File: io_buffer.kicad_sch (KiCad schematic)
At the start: 68 parts, among them J15 Conn_01x08, J5 IDC-Header_2x10_P2.54mm, J6 Conn_01x08, U13 SN74LVC1T45DCKR, U14 SN74LVC1T45DCKR, U15 SN74LVC1T45DCKR, U16 SN74LVC1T45DCKR, U17 SN74LVC1T45DCKR, U18 PCA6408APW, U19 TPS73101DBV, U20 DAC081C081CIMK, U21 INA233, U6 SN74LVC1T45DCKR, U7 SN74LVC1T45DCKR, U8 SN74LVC1T45DCKR

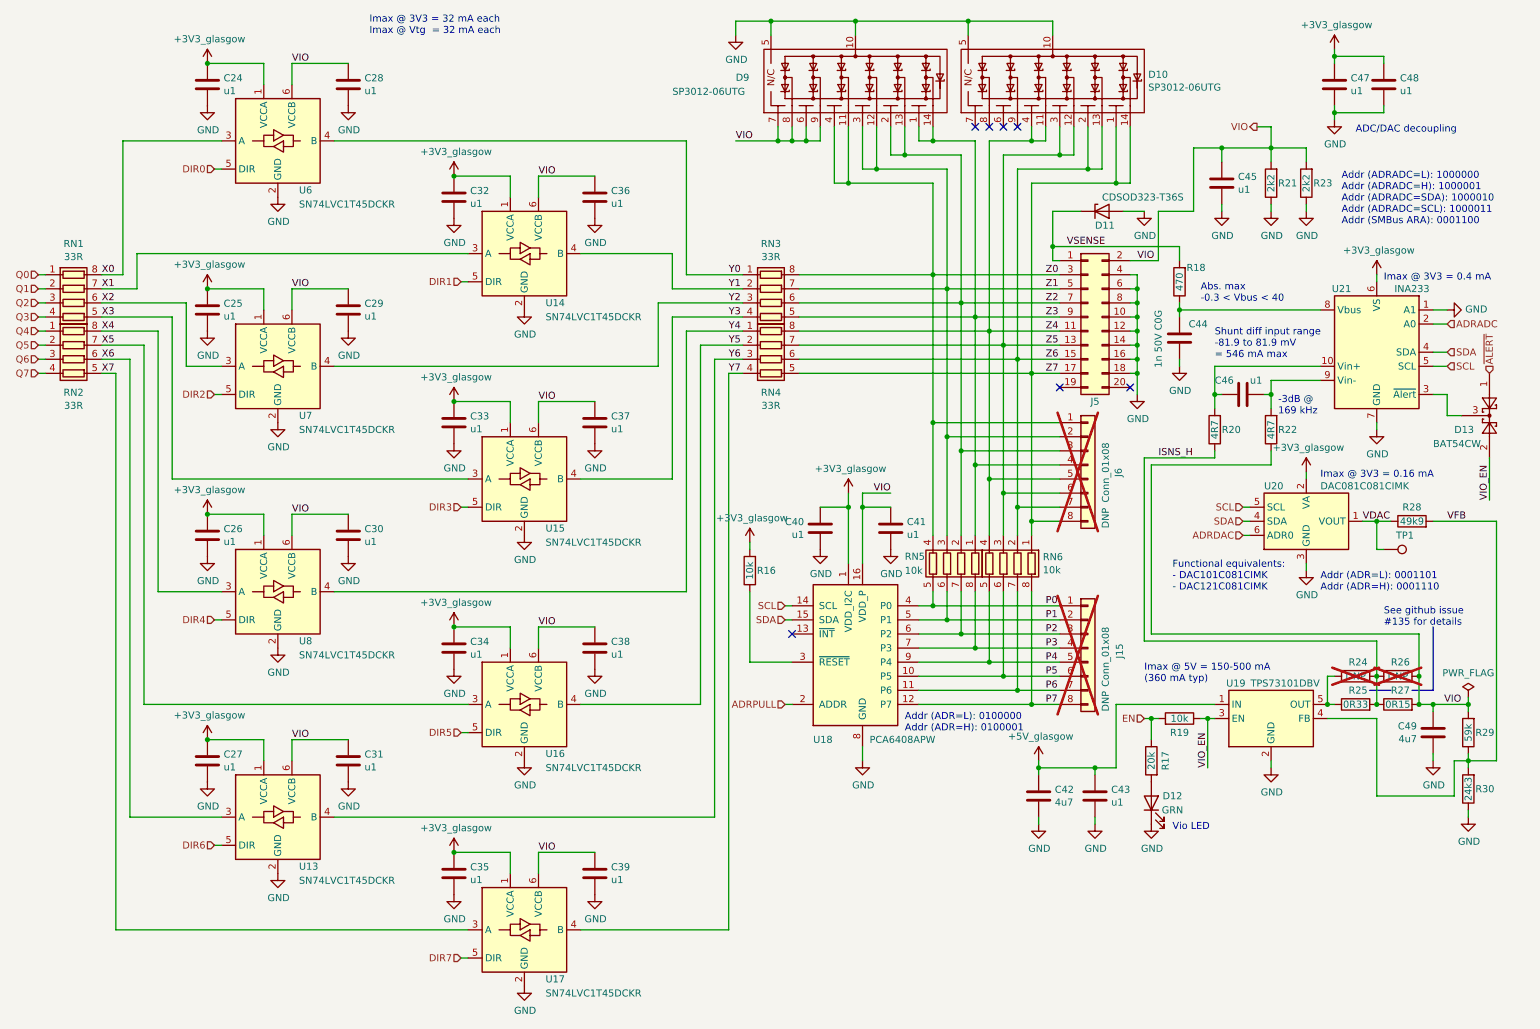
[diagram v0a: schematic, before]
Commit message: finished schematic draft and started placing components
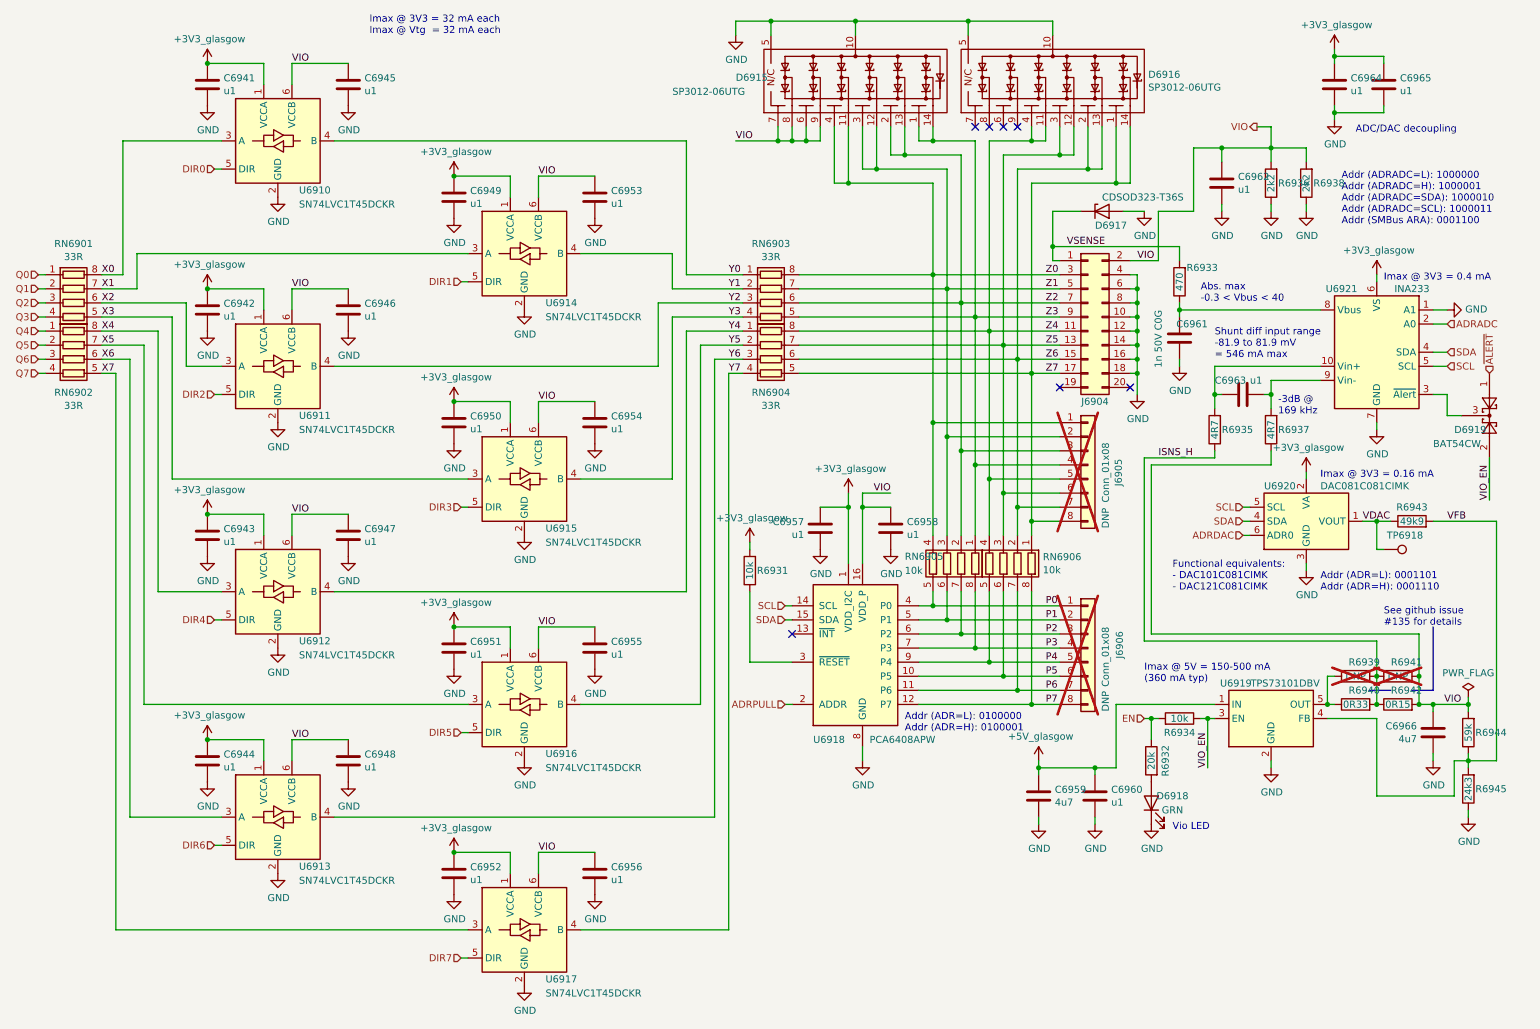
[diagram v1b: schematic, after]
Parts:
- renumbered C24 to C6941, C25 to C6942, C26 to C6943, C27 to C6944, C28 to C6945, C29 to C6946, C30 to C6947, C31 to C6948, C32 to C6949, C33 to C6950, C34 to C6951, C35 to C6952, C36 to C6953, C37 to C6954, C38 to C6955, C39 to C6956, C40 to C6957, C41 to C6958, C42 to C6959, C43 to C6960, C44 to C6961, C45 to C6962, C46 to C6963, C47 to C6964, C48 to C6965, C49 to C6966, D9 to D6915, D10 to D6916, D11 to D6917, D12 to D6918, D13 to D6919, J5 to J6904, J6 to J6905, J15 to J6906, R16 to R6931, R17 to R6932, R18 to R6933, R19 to R6934, R20 to R6935, R21 to R6936, R22 to R6937, R23 to R6938, R24 to R6939, R25 to R6940, R26 to R6941, R27 to R6942, R28 to R6943, R29 to R6944, R30 to R6945, RN1 to RN6901, RN2 to RN6902, RN3 to RN6903, RN4 to RN6904, RN5 to RN6905, RN6 to RN6906, TP1 to TP6918, U6 to U6910, U7 to U6911, U8 to U6912, U13 to U6913, U14 to U6914, U15 to U6915, U16 to U6916, U17 to U6917, U18 to U6918, U19 to U6919, U20 to U6920, U21 to U6921

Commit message: commit before removing duplicated glasgow
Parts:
- U38: renamed from U6921; footprint Glasgow:VSSOP-10_3x3mm_P0.5mm -> Package_SO:VSSOP-10_3x3mm_P0.5mm
- renumbered C6941 to C134, C6942 to C135, C6943 to C136, C6944 to C137, C6945 to C138, C6946 to C139, C6947 to C140, C6948 to C141, C6949 to C142, C6950 to C143, C6951 to C144, C6952 to C145, C6953 to C146, C6954 to C147, C6955 to C148, C6956 to C149, C6957 to C150, C6958 to C151, C6959 to C152, C6960 to C153, C6961 to C154, C6962 to C155, C6963 to C156, C6964 to C157, C6965 to C158, C6966 to C159, D6915 to D22, D6916 to D23, D6917 to D24, D6918 to D25, D6919 to D26, J6904 to J28, J6905 to J29, J6906 to J30, R6931 to R71, R6932 to R72, R6933 to R73, R6934 to R74, R6935 to R75, R6936 to R76, R6937 to R77, R6938 to R78, R6939 to R79, R6940 to R80, R6941 to R81, R6942 to R82, R6943 to R83, R6944 to R84, R6945 to R85, RN6901 to RN1, RN6902 to RN2, RN6903 to RN3, RN6904 to RN4, RN6905 to RN5, RN6906 to RN6, TP6918 to TP21, U6910 to U27, U6911 to U28, U6912 to U29, U6913 to U30, U6914 to U31, U6915 to U32, U6916 to U33, U6917 to U34, U6918 to U35, U6919 to U36, U6920 to U37

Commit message: added USB-C
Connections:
- net GND: no longer C155.2
- new net GD: C155.2
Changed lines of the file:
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@@
 			)
 		)
-		(property "Value" "GND"
+		(property "Value" "GD"
 			(at 233.807 53.9242 0)
 			(show_name no)

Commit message: added MPN to all parts by hand :'(
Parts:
- C134, C135, C136, C137, C138, C139, C140, C141, C142, C143, C144, C145, C146, C147, C148, C149, C150, C151, C153, C155, C156, C157, C158: MPN TMK105BJ104KV-F -> C1005X7R1H104K050BE
- C152, C159: footprint Capacitor_SMD:C_0603_1608Metric -> A_DFRobot:C_0805_2012Metric; 1b2-bom-key cap-cer-0603-4u7 -> (none); MPN LMK107BJ475KAHT -> GRM21BR61H475KE51L; Mfg Taiyo Yuden -> (none)
- R71: 1b2-bom-key res-0402-10k -> (none); MPN RC0402FR-1310KL -> RCS040210K0FKED; Mfg Yageo -> (none)
- R73: MPN RC0402FR-07470RL -> ERJ-2RKF4700X
- R74: MPN RC0402FR-1310KL -> RCS040210K0FKED
- R76, R78: MPN RC0402FR-132K2L -> RCS04022K20FKED
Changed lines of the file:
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@@
 			)
 		)
-		(property "MPN" "TMK105BJ104KV-F"
+		(property "MPN" "C1005X7R1H104K050BE"
 			(at 93.98 280.67 0)
 			(hide yes)
@@
 			)
 		)
-		(property "MPN" "TMK105BJ104KV-F"
+		(property "MPN" "C1005X7R1H104K050BE"
 			(at 134.62 64.77 0)
 			(hide yes)
@@
 			)
 		)
-		(property "MPN" "TMK105BJ104KV-F"
+		(property "MPN" "C1005X7R1H104K050BE"
 			(at 134.62 64.77 0)
 			(hide yes)
@@
 			)
 		)
-		(property "MPN" "TMK105BJ104KV-F"
+		(property "MPN" "C1005X7R1H104K050BE"
 			(at 149.86 82.55 0)
 			(hide yes)
@@
 			)
 		)
-		(property "MPN" "TMK105BJ104KV-F"
+		(property "MPN" "C1005X7R1H104K050BE"
 			(at -12.7 64.77 0)
 			(hide yes)
@@
 			)
 		)
-		(property "MPN" "TMK105BJ104KV-F"
+		(property "MPN" "C1005X7R1H104K050BE"
 			(at 12.7 64.77 0)
 			(hide yes)
@@
 			)
 		)
-		(property "MPN" "TMK105BJ104KV-F"
+		(property "MPN" "C1005X7R1H104K050BE"
 			(at -12.7 105.41 0)
 			(hide yes)
@@
 			)
 		)
-		(property "MPN" "TMK105BJ104KV-F"
+		(property "MPN" "C1005X7R1H104K050BE"
 			(at 12.7 105.41 0)
 			(hide yes)
@@
 			)
 		)
-		(property "MPN" "TMK105BJ104KV-F"
+		(property "MPN" "C1005X7R1H104K050BE"
 			(at -12.7 146.05 0)
 			(hide yes)
@@
 			)
 		)
-		(property "MPN" "TMK105BJ104KV-F"
+		(property "MPN" "C1005X7R1H104K050BE"
 			(at 12.7 146.05 0)
 			(hide yes)
@@
 			)
 		)
-		(property "MPN" "TMK105BJ104KV-F"
+		(property "MPN" "C1005X7R1H104K050BE"
 			(at -12.7 186.69 0)
 			(hide yes)
@@
 			)
 		)
-		(property "MPN" "TMK105BJ104KV-F"
+		(property "MPN" "C1005X7R1H104K050BE"
 			(at 12.7 186.69 0)
 			(hide yes)
@@
 			)
 		)
-		(property "MPN" "TMK105BJ104KV-F"
+		(property "MPN" "C1005X7R1H104K050BE"
 			(at 31.75 85.09 0)
 			(hide yes)
@@
 			)
 		)
-		(property "MPN" "TMK105BJ104KV-F"
+		(property "MPN" "C1005X7R1H104K050BE"
 			(at 57.15 85.09 0)
 			(hide yes)
@@
 			)
 		)
-		(property "MPN" "TMK105BJ104KV-F"
+		(property "MPN" "C1005X7R1H104K050BE"
 			(at 31.75 125.73 0)
 			(hide yes)
@@
 			)
 		)
-		(property "MPN" "TMK105BJ104KV-F"
+		(property "MPN" "C1005X7R1H104K050BE"
 			(at 57.15 125.73 0)
 			(hide yes)
@@
 			)
 		)
-		(property "MPN" "TMK105BJ104KV-F"
+		(property "MPN" "C1005X7R1H104K050BE"
 			(at 31.75 166.37 0)
 			(hide yes)
@@
 			)
 		)
-		(property "MPN" "TMK105BJ104KV-F"
+		(property "MPN" "C1005X7R1H104K050BE"
 			(at 57.15 166.37 0)
 			(hide yes)
@@
 			)
 		)
-		(property "MPN" "TMK105BJ104KV-F"
+		(property "MPN" "C1005X7R1H104K050BE"
 			(at 31.75 207.01 0)
 			(hide yes)
@@
 			)
 		)
-		(property "MPN" "TMK105BJ104KV-F"
+		(property "MPN" "C1005X7R1H104K050BE"
 			(at 57.15 207.01 0)
 			(hide yes)
@@
 			)
 		)
-		(property "MPN" "RC0402FR-132K2L"
+		(property "MPN" "RCS04022K20FKED"
 			(at 398.78 -81.28 0)
 			(hide yes)
@@
 			)
 		)
-		(property "MPN" "TMK105BJ104KV-F"
+		(property "MPN" "C1005X7R1H104K050BE"
 			(at 245.11 144.78 0)
 			(hide yes)
@@
 			)
 		)
-		(property "Datasheet" "https://www.mouser.com/datasheet/2/447/PYu-RC_Group_51_RoHS_L_10-1527934.pdf"
+		(property "Datasheet" ""
 			(at 148.59 114.3 0)
 			(hide yes)
@@
 			)
 		)
-		(property "Mfg" "Yageo"
+		(property "Mfg" ""
 			(at 259.08 31.75 0)
 			(hide yes)
@@
 			)
 		)
-		(property "MPN" "RC0402FR-1310KL"
+		(property "MPN" "RCS040210K0FKED"
 			(at 259.08 31.75 0)
 			(hide yes)
@@
 			)
 		)
-		(property "1b2-bom-key" "res-0402-10k"
+		(property "1b2-bom-key" ""
 			(at 148.59 114.3 0)
 			(hide yes)
@@
 			)
 		)
-		(property "Footprint" "Capacitor_SMD:C_0603_1608Metric"
+		(property "Footprint" "A_DFRobot:C_0805_2012Metric"
 			(at 270.8148 147.32 0)
 			(hide yes)
@@
 			)
 		)
-		(property "Datasheet" "https://www.mouser.com/datasheet/2/400/lcc_commercial_general_en-837201.pdf"
+		(property "Datasheet" ""
 			(at 271.78 143.51 0)
 			(hide yes)
@@
 			)
 		)
-		(property "Mfg" "Taiyo Yuden"
+		(property "Mfg" ""
 			(at 355.6 181.61 0)
 			(hide yes)
@@
 			)
 		)
-		(property "MPN" "LMK107BJ475KAHT"
+		(property "MPN" "GRM21BR61H475KE51L"
 			(at 355.6 181.61 0)
 			(hide yes)
@@
 			)
 		)
-		(property "1b2-bom-key" "cap-cer-0603-4u7"
+		(property "1b2-bom-key" ""
 			(at 271.78 143.51 0)
 			(hide yes)
@@
 			)
 		)
-		(property "Footprint" "Capacitor_SMD:C_0603_1608Metric"
+		(property "Footprint" "A_DFRobot:C_0805_2012Metric"
 			(at 201.6252 158.75 0)
 			(hide yes)
@@
 			)
 		)
-		(property "Datasheet" "https://www.mouser.com/datasheet/2/400/lcc_commercial_general_en-837201.pdf"
+		(property "Datasheet" ""
 			(at 200.66 154.94 0)
 			(hide yes)
@@
 			)
 		)
-		(property "Mfg" "Taiyo Yuden"
+		(property "Mfg" ""
 			(at 116.84 193.04 0)
 			(hide yes)
@@
 			)
 		)
-		(property "MPN" "LMK107BJ475KAHT"
+		(property "MPN" "GRM21BR61H475KE51L"
 			(at 116.84 193.04 0)
 			(hide yes)
@@
 			)
 		)
-		(property "1b2-bom-key" "cap-cer-0603-4u7"
+		(property "1b2-bom-key" ""
 			(at 200.66 154.94 0)
 			(hide yes)
@@
 			)
 		)
-		(property "MPN" "TMK105BJ104KV-F"
+		(property "MPN" "C1005X7R1H104K050BE"
 			(at 90.17 144.78 0)
 			(hide yes)
@@
 			)
 		)
-		(property "MPN" "TMK105BJ104KV-F"
+		(property "MPN" "C1005X7R1H104K050BE"
 			(at 199.39 -1.27 0)
 			(hide yes)
@@
 			)
 		)
-		(property "MPN" "RC0402FR-132K2L"
+		(property "MPN" "RCS04022K20FKED"
 			(at 405.13 -81.28 0)
 			(hide yes)
@@
 			)
 		)
-		(property "MPN" "RC0402FR-1310KL"
+		(property "MPN" "RCS040210K0FKED"
 			(at 198.12 392.43 0)
 			(hide yes)
@@
 			)
 		)
-		(property "MPN" "RC0402FR-07470RL"
+		(property "MPN" "ERJ-2RKF4700X"
 			(at 382.27 -63.5 0)
 			(hide yes)

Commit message: Prototype
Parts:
- D22: value SP3012-06UTG -> TPD6E05U06RVZR; 1b2-bom-key diode-14udfn-sp3012-06utg -> (none); MPN SP3012-06UTG -> TPD6E05U06RVZR; Mfg Littlefuse -> (none)
- D23: value SP3012-06UTG -> TPD6E05U06RVZR; MPN SP3012-06UTG -> TPD6E05U06RVZR; Mfg Littlefuse -> (none)
- J28: footprint Connector_IDC:IDC-Header_2x10_P2.54mm_Vertical -> Connector_IDC:IDC-Header_2x10_P2.54mm_Horizontal
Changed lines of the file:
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@@
 			)
 		)
-		(property "Footprint" "Connector_IDC:IDC-Header_2x10_P2.54mm_Vertical"
+		(property "Footprint" "Connector_IDC:IDC-Header_2x10_P2.54mm_Horizontal"
 			(at 209.55 68.58 0)
 			(hide yes)
@@
 			)
 		)
-		(property "Value" "SP3012-06UTG"
+		(property "Value" "TPD6E05U06RVZR"
 			(at 220.4212 27.178 0)
 			(show_name no)
@@
 			)
 		)
-		(property "Datasheet" "https://www.littelfuse.com/~/media/electronics/datasheets/tvs_diode_arrays/littelfuse_tvs_diode_array_sp3012_datasheet.pdf.pdf"
+		(property "Datasheet" ""
 			(at 194.945 26.035 0)
 			(hide yes)
@@
 			)
 		)
-		(property "MPN" "SP3012-06UTG"
+		(property "MPN" "TPD6E05U06RVZR"
 			(at 203.2 25.4 0)
 			(hide yes)
@@
 			)
 		)
-		(property "Mfg" "Littlefuse"
+		(property "Mfg" ""
 			(at 203.2 25.4 0)
 			(hide yes)
@@
 			)
 		)
-		(property "Value" "SP3012-06UTG"
+		(property "Value" "TPD6E05U06RVZR"
 			(at 134.62 27.94 0)
 			(show_name no)
@@
 			)
 		)
-		(property "Datasheet" "https://www.littelfuse.com/~/media/electronics/datasheets/tvs_diode_arrays/littelfuse_tvs_diode_array_sp3012_datasheet.pdf.pdf"
+		(property "Datasheet" ""
 			(at 159.385 26.035 0)
 			(hide yes)
@@
 			)
 		)
-		(property "1b2-bom-key" "diode-14udfn-sp3012-06utg"
+		(property "1b2-bom-key" ""
 			(at 167.64 25.4 0)
 			(hide yes)
@@
 			)
 		)
-		(property "MPN" "SP3012-06UTG"
+		(property "MPN" "TPD6E05U06RVZR"
 			(at 167.64 25.4 0)
 			(hide yes)
@@
 			)
 		)
-		(property "Mfg" "Littlefuse"
+		(property "Mfg" ""
 			(at 167.64 25.4 0)
 			(hide yes)
